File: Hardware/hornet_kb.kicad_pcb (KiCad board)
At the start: 2 copper layers, 195.1 x 100.9 mm, 149 parts, among them J1 Conn_ST_STDC14, J10 USB_C_Receptacle_USB2.0, J2 Conn_01x03, SW1 ESC, SW10 TAB, SW11 Q, SW12 W, SW13 E, SW14 R, SW15 T, SW17 M1, SW18 CAPS, SW19 A, SW2 `, SW20 S, SW21 D, SW22 F, SW23 G, SW25 M2, SW26 M3, SW27 SW_DPDT_x2, SW28 SHIFT, SW29 CTRL, SW3 1, SW30 Rot_Enc, SW31 Z, SW32 WIN, SW34 X, SW35 FN, SW37 C, SW38 ALT, SW4 2, SW40 V, SW41 SPACE, SW43 B, SW44 DEL, SW5 3, SW6 4, SW7 5, SW8 6, SW9 M0, SW98 SW_Push, U1 nRF52840, U2 BQ24040, U3 BQ51050BRHL, U4 AP22814BW5, U5 TPS2116DRL, Y1 32.768kHz, Y2 32MHz

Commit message: Finished draft placement of parts
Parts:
- removed R11: 1k, Resistor_SMD:R_0603_1608Metric
- removed R17: 20k, Resistor_SMD:R_0603_1608Metric
- removed Y2: 32MHz, Crystal:Crystal_SMD_2016-4Pin_2.0x1.6mm
- added D33: LED, LED_SMD:LED_0805_2012Metric, F.Cu at (208.2, 78.0)
- added IFA1: ~, RF_Antenna:Texas_SWRA117D_2.4GHz_Right, F.Cu at (223.2, 96.4)
- added Y3: Crystal_GND24, Crystal:Crystal_SMD_2016-4Pin_2.0x1.6mm, F.Cu at (225.6, 84.6)
- JP2: moved to B.Cu
- moved R16 94.6 mm to (212.3, 91.4), turned to 90 degrees
- moved C8 94.5 mm to (204.0, 98.5)
- moved L3 76.3 mm to (214.7, 75.6), turned to -90 degrees
- moved C25 72.6 mm to (221.5, 54.7), turned to 180 degrees
- moved D99 72.1 mm to (202.8, 77.8), turned to 90 degrees
- moved C14 71.2 mm to (209.5, 104.0)
- moved C15 70.8 mm to (205.2, 104.0)
- moved C16 69.3 mm to (207.5, 100.7), turned to 0 degrees
- moved R6 69.0 mm to (203.3, 73.6), turned to -90 degrees
- moved C13 68.9 mm to (203.4, 100.8)
- moved C24 68.8 mm to (207.0, 57.1), turned to -90 degrees
- moved C19 68.4 mm to (208.9, 91.4)
- moved C27 68.0 mm to (203.3, 91.4), turned to -90 degrees
- moved C20 67.6 mm to (206.0, 91.4)
- moved U3 67.2 mm to (208.5, 96.2)
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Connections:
- C28 pad 2: VSS_pa -> VSS_PA
- C29 pad 2: GND -> VSS_PA
- NT1 pad 1: VSS_pa -> VSS_PA
- R13 pad 1: NRF_ANTENNA -> Net-(IFA1-ANT)
- U1 pad AC21: /R_COL_2 -> unconnected-(U1-P0.25-PadAC21)
- U1 pad AD10: /R_COL_7 -> unconnected-(U1-P0.15-PadAD10)
- U1 pad AD12: /R_COL_6 -> unconnected-(U1-P0.17-PadAD12)
- U1 pad AD16: /R_ROW_2 -> unconnected-(U1-P0.20-PadAD16)
- U1 pad AD18: /R_COL_5 -> unconnected-(U1-P0.22-PadAD18)
- U1 pad AD20: /R_COL_4 -> unconnected-(U1-P0.24-PadAD20)
- U1 pad AD8: /R_ROW_0 -> unconnected-(U1-P0.13-PadAD8)
- U1 pad F23: VSS_pa -> VSS_PA
- U1 pad G1: /R_COL_1 -> unconnected-(U1-P0.26-PadG1)
- U1 pad H2: /R_COL_0 -> unconnected-(U1-P0.27-PadH2)
- U1 pad P2: /Rotary_L -> unconnected-(U1-P1.08-PadP2)
- U1 pad P23: /Rotary_R -> unconnected-(U1-P1.07-PadP23)
- U1 pad R1: /Rotary_SW -> unconnected-(U1-TRACEDATA3/P1.09-PadR1)
- U1 pad T23: /R_ROW_4 -> unconnected-(U1-P1.05-PadT23)
- U1 pad U24: /R_ROW_3 -> unconnected-(U1-P1.04-PadU24)
- U1 pad W24: /R_ROW_1 -> unconnected-(U1-P1.02-PadW24)
- U5 pad 1: Net-(U5-GND) -> GND
- U5 pad 4: Net-(U5-PR1) -> VBUS
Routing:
- net GND: track 0.00 -> 42.6 mm
- net Net-(C13-Pad1): track 0.00 -> 38.0 mm
- net VBUS: track 0.00 -> 23.9 mm, vias 0 -> 2
- net Net-(U3-AC2): track 0.00 -> 23.9 mm
- net VDDH: track 0.00 -> 16.3 mm
- net VDD: track 0.00 -> 11.3 mm
- net Net-(U1-XC1): track 0.00 -> 7.42 mm
- net /ANT: track 0.00 -> 7.23 mm
- net Net-(U1-DEC1): track 0.00 -> 7.07 mm
- net Net-(C29-Pad1): track 0.00 -> 6.23 mm
- net Net-(U1-XL1/P0.00): track 0.00 -> 6.23 mm
- net Net-(U1-XL2/P0.01): track 0.00 -> 6.09 mm
- net Net-(U1-XC2): track 0.00 -> 5.94 mm
- net Net-(U1-DEC4): track 0.00 -> 4.58 mm
- net Net-(U1-DCCH): track 0.00 -> 3.36 mm
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- added copper zone on In1.Cu, net VBUS
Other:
- board size 195.1 x 100.9 mm -> 193 x 100.3 mm
- copper layers 2 -> 4

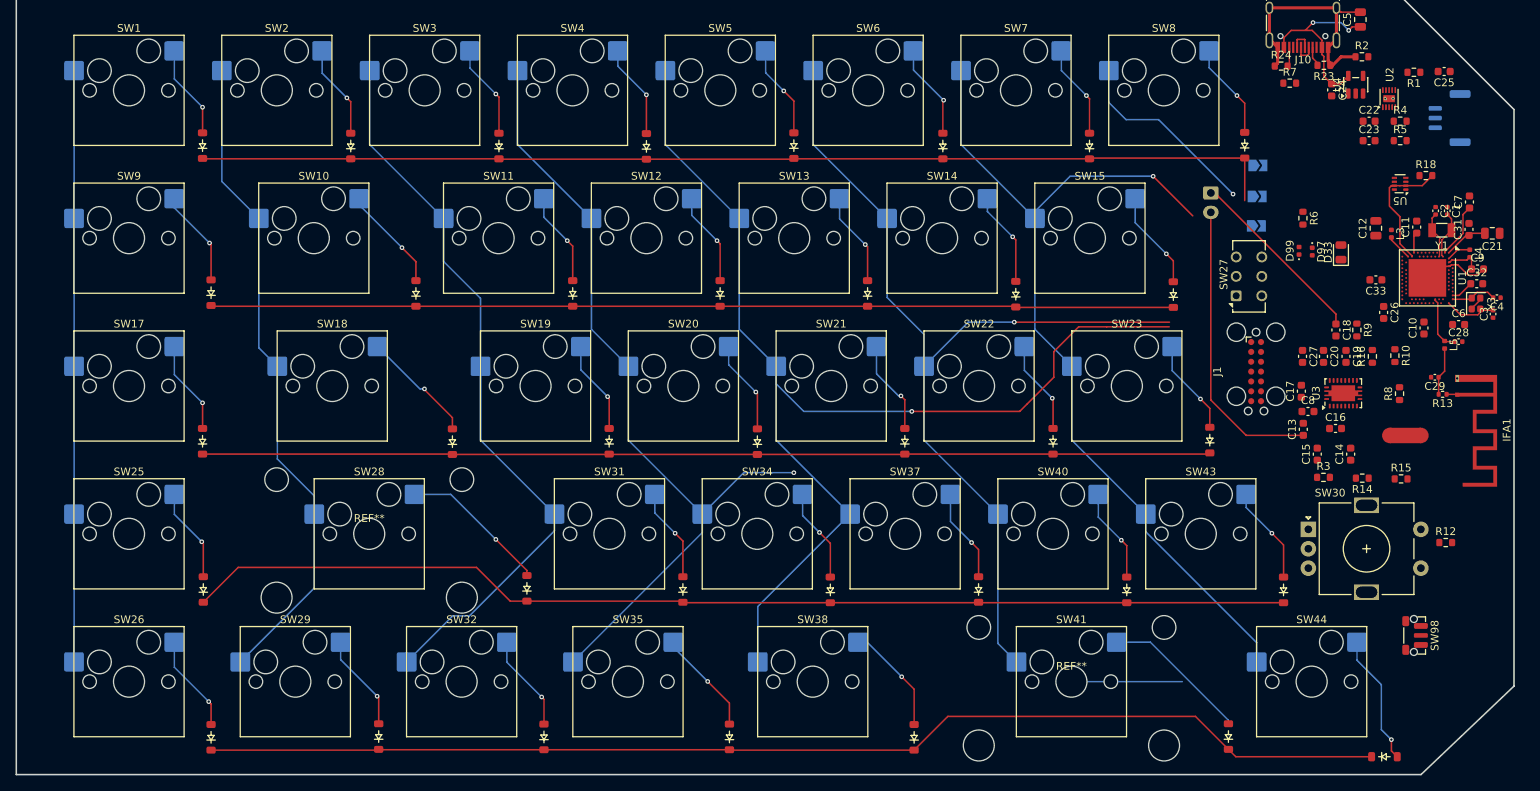
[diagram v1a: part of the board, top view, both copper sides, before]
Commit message: Update footprints and positions for multiple components
Changed footprints, positions, and orientations for several components including LEDs, capacitors, net ties, ICs, and antenna in hornet_kb.kicad_pcb. These updates improve layout accuracy and reflect changes in component selection and placement for better manufacturability and electrical performance.
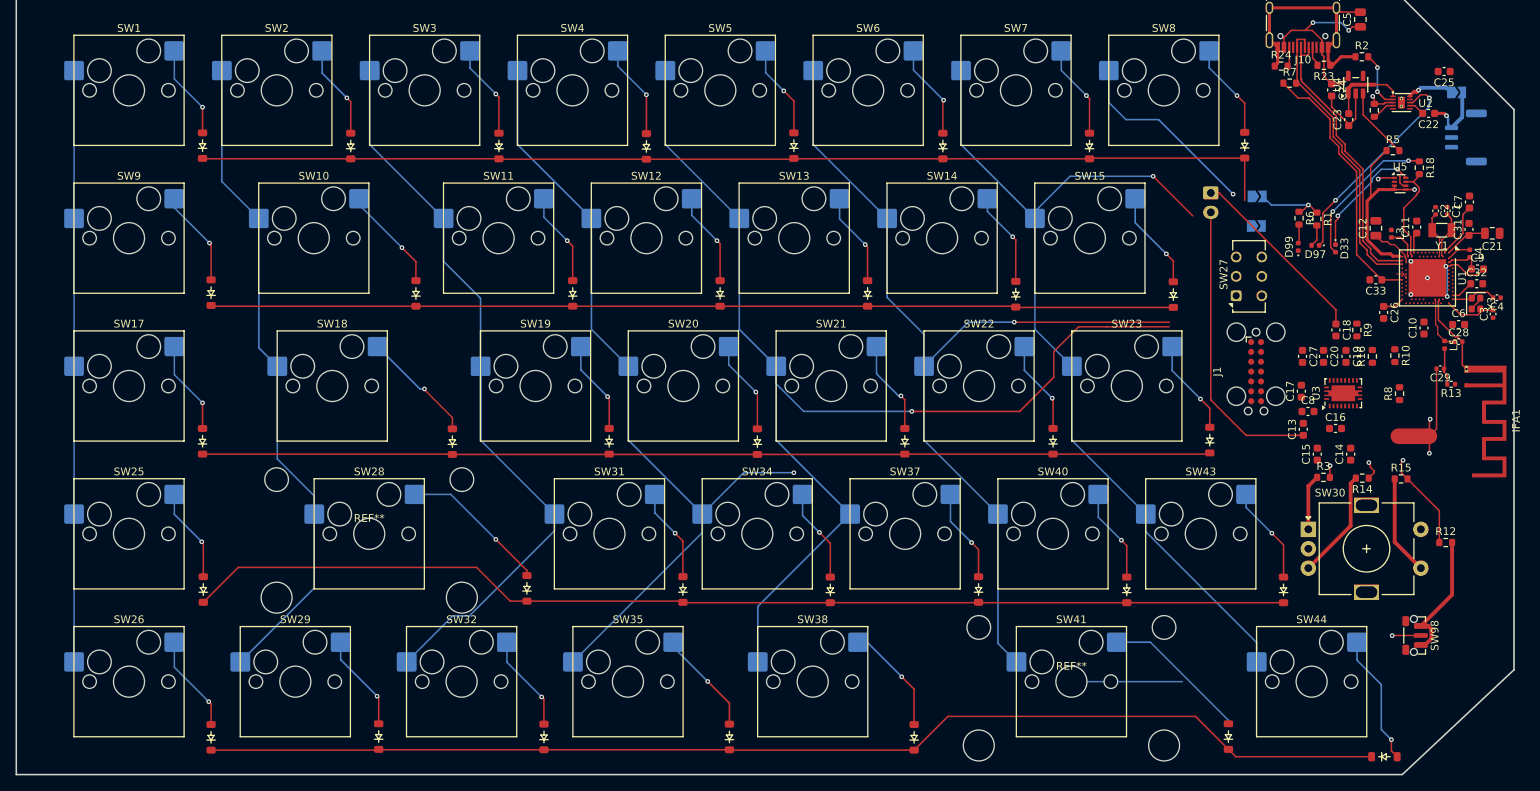
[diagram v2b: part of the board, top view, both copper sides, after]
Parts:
- D33: footprint LED_SMD:LED_0805_2012Metric -> LED_SMD:LED_0402_1005Metric
- moved JP2 27.3 mm to (223.1, 57.4)
- moved R1 22.7 mm to (205.1, 73.7), turned to -90 degrees
- moved C22 7.74 mm to (219.5, 60.1), turned to 180 degrees
- moved C23 3.77 mm to (209.2, 60.9), turned to 90 degrees
- moved R4 3.62 mm to (212.5, 59.7), turned to -90 degrees
- moved J2 3.26 mm to (224.3, 63.2)
- moved R13 1.70 mm to (222.4, 95.0)
- moved IFA1 1.70 mm to (224.4, 95.2)
- moved U2 1.68 mm to (216.0, 58.7), turned to 0 degrees
- moved R5 1.59 mm to (214.9, 64.9)
- moved R18 1.32 mm to (218.3, 67.1), turned to -90 degrees
- moved C29 1.30 mm to (221.0, 93.0)
- moved NT1 1.10 mm to (217.6, 101.7)
- moved D97 0.89 mm to (204.9, 77.1), turned to 180 degrees
- moved D33 0.86 mm to (207.5, 77.5), turned to -90 degrees
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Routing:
- net VDD: track 11.3 -> 64.9 mm, vias 0 -> 3
- net GND: track 42.6 -> 79.8 mm, vias 0 -> 8
- net /D+: track 2.99 -> 38.8 mm
- net /D-: track 2.93 -> 37.7 mm
- net Net-(D97-K): track 0.00 -> 28.0 mm, vias 0 -> 2
- net VBUS: track 23.9 -> 48.4 mm, vias 2 -> 3
- net VSS_PA: track 0.00 -> 24.2 mm, vias 0 -> 2
- net Net-(D33-A): track 0.00 -> 19.5 mm, vias 0 -> 2
- net /~{RESET}: track 0.00 -> 18.3 mm
- net +BATT: track 0.00 -> 18.0 mm, vias 0 -> 2
- net Net-(D33-K): track 0.00 -> 15.8 mm, vias 0 -> 2
- net /Rotary_R: track 0.00 -> 14.1 mm
- net /Rotary_SW: track 0.00 -> 12.9 mm
- net Net-(U2-IN): track 0.00 -> 10.2 mm
- net Net-(U4-~{FLG}): track 0.00 -> 9.32 mm
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- added copper zone on In2.Cu, net GND
- added copper zone on In2.Cu, net VSS_PA
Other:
- outline, holes or cut-outs redrawn

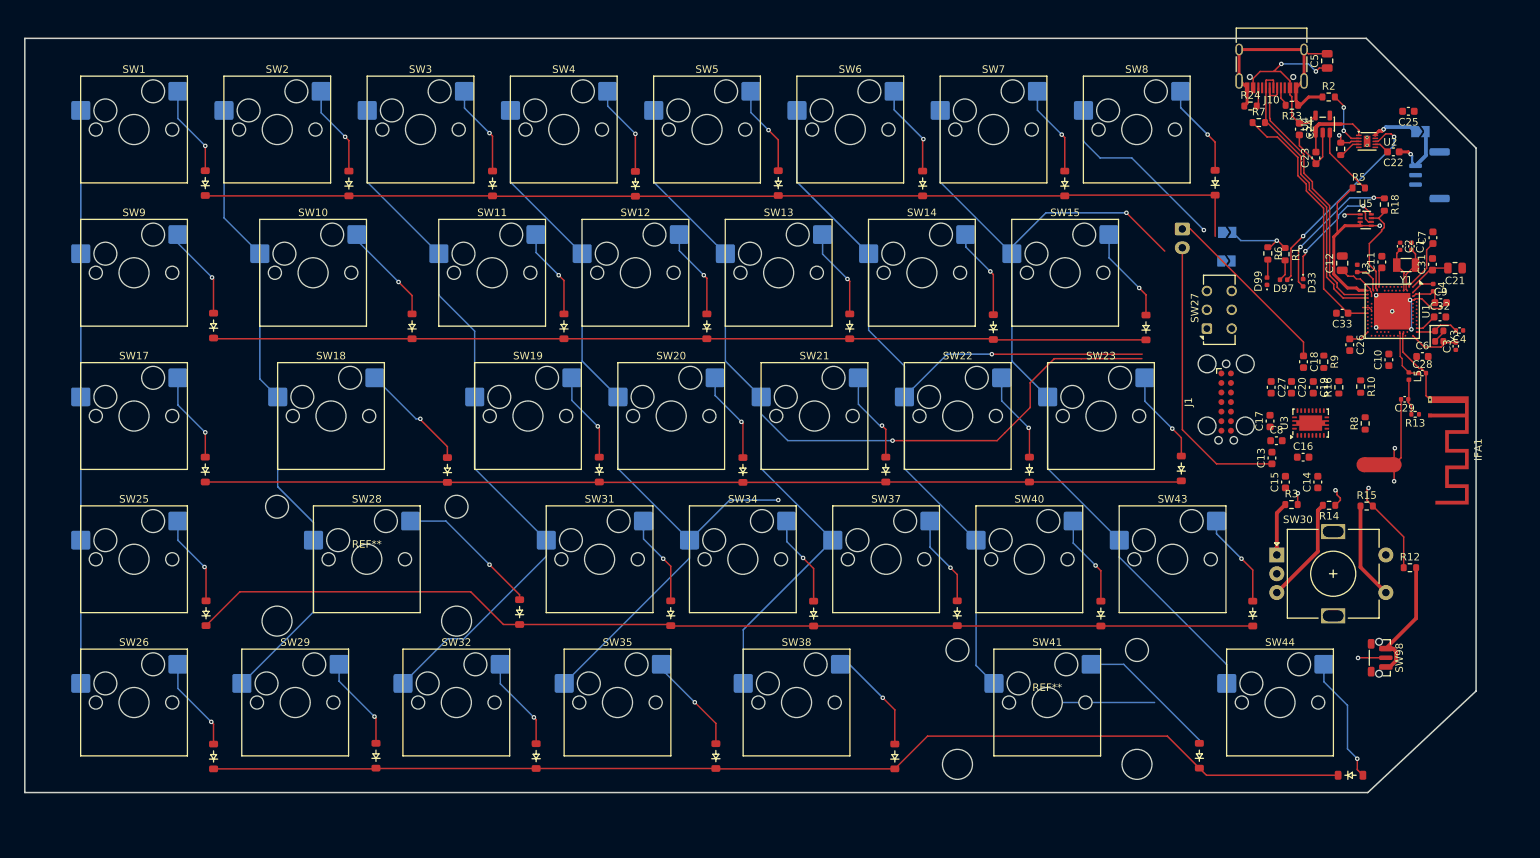
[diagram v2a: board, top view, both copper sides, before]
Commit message: Completed mcu routing
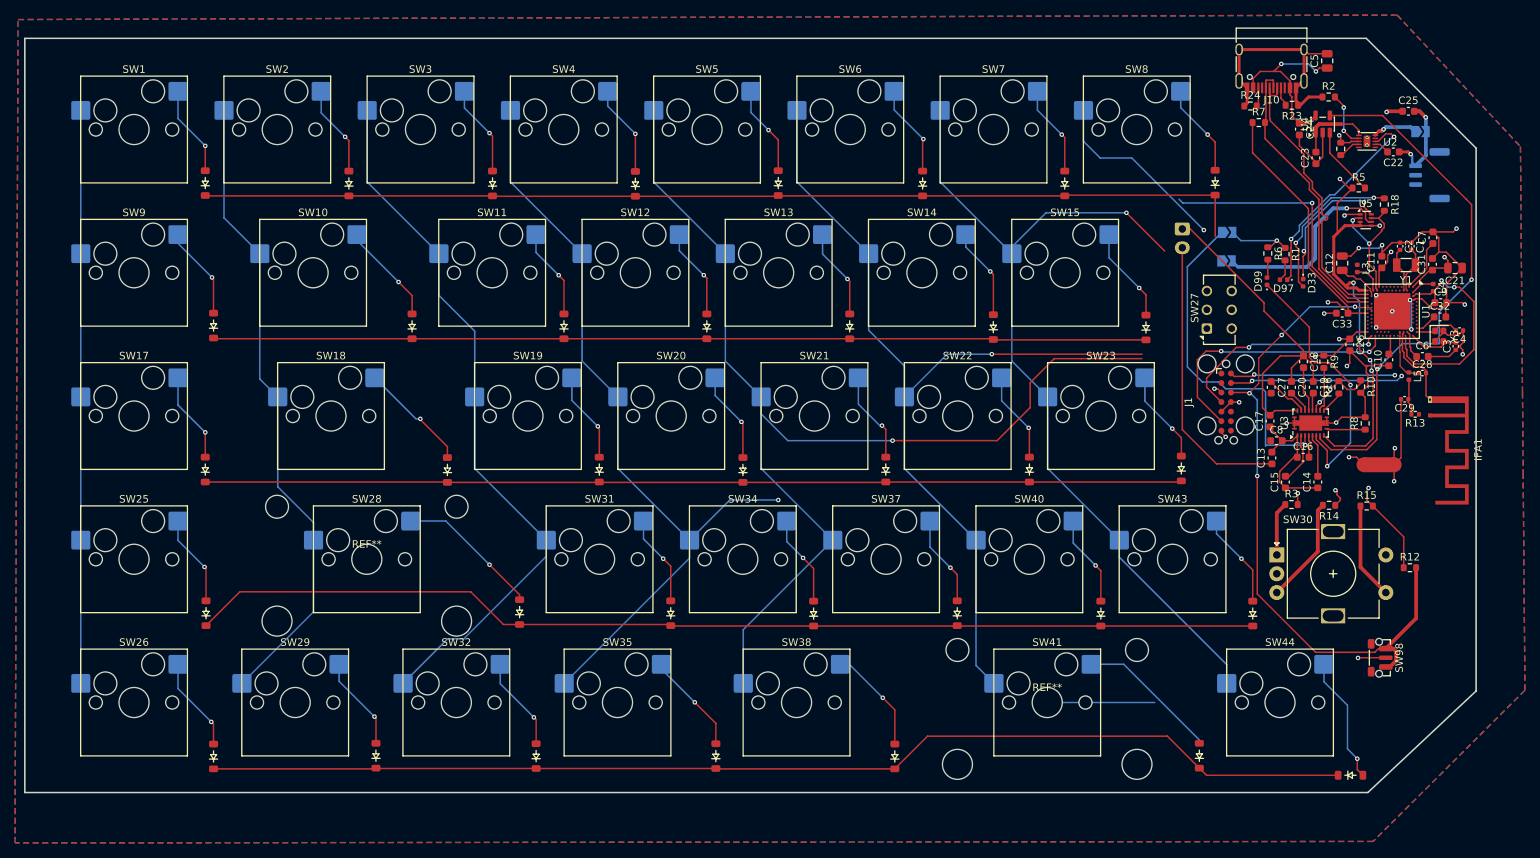
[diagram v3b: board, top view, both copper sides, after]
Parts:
- turned C25 to 0 degrees
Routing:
- net GND: track 79.8 -> 169.1 mm, vias 8 -> 21
- net Net-(U3-~{AD-EN}): track 0.00 -> 72.3 mm, vias 0 -> 2
- net /~{RESET}: track 18.3 -> 90.5 mm, vias 0 -> 4
- net Net-(JP3-A): track 0.00 -> 45.4 mm, vias 0 -> 1
- net Net-(D99-K): track 0.00 -> 35.8 mm, vias 0 -> 2
- net unconnected-(U1-P0.13-PadAD8): track 0.00 -> 35.7 mm, vias 0 -> 1
- net /PRG_CLK: track 0.00 -> 35.3 mm, vias 0 -> 2
- net VBUS: track 48.4 -> 81.1 mm, vias 3 -> 8
- net /PRC_DIO: track 0.00 -> 29.0 mm, vias 0 -> 2
- net Net-(U1-DEC4): track 4.58 -> 31.2 mm, vias 0 -> 2
- net Net-(U3-AC2): track 24.2 -> 48.5 mm
- net +VDC: track 2.11 -> 25.8 mm, vias 0 -> 1
- net /COMPRT_RX: track 0.00 -> 23.1 mm, vias 0 -> 2
- net /COMPRT_TX: track 0.00 -> 22.1 mm, vias 0 -> 2
- net Net-(U3-AC1): track 0.00 -> 19.8 mm
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- added copper zone on B.Cu, net GND
- added copper zone on F.Cu, net GND
- added copper zone on In1.Cu, net VDD

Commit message: FINISHED FIRST DRAFT OF LAYOUT!!
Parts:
- added JP4: PWR_SWITCH, Jumper:SolderJumper-2_P1.3mm_Open_TrianglePad1.0x1.5mm, B.Cu at (191.9, 78.2)
- SW27: footprint Button_Switch_THT:SW_CK_JS202011CQN_DPDT_Straight -> ScottoKeebs_Miscellaneous:SW_CK_JS202011CQN_DPDT_Straight
- moved JP1 9.39 mm to (204.6, 68.7)
- moved D99 7.36 mm to (209.0, 81.1)
- moved R6 6.25 mm to (206.0, 79.0), turned to -45 degrees
- moved D97 4.12 mm to (208.5, 79.1), turned to -45 degrees
- moved D33 2.73 mm to (210.0, 78.6), turned to -45 degrees
- moved JP3 2.51 mm to (198.4, 68.5)
- moved J1 2.35 mm to (197.3, 95.7)
- moved R1 1.61 mm to (205.9, 75.1)
- moved SW27 1.14 mm to (195.0, 84.7)
- moved L1 0.16 mm to (191.5, 70.2)
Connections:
- D10 pad 1: /R_ROW_2 -> /R_ROW_1
- D11 pad 1: /R_ROW_2 -> /R_ROW_1
- D12 pad 1: /R_ROW_2 -> /R_ROW_1
- D13 pad 1: /R_ROW_2 -> /R_ROW_1
- D14 pad 1: /R_ROW_2 -> /R_ROW_1
- D15 pad 1: /R_ROW_2 -> /R_ROW_1
- D17 pad 1: /R_ROW_1 -> /R_ROW_2
- D18 pad 1: /R_ROW_1 -> /R_ROW_2
- D19 pad 1: /R_ROW_1 -> /R_ROW_2
- D20 pad 1: /R_ROW_1 -> /R_ROW_2
- D21 pad 1: /R_ROW_1 -> /R_ROW_2
- D22 pad 1: /R_ROW_1 -> /R_ROW_2
- D23 pad 1: /R_ROW_1 -> /R_ROW_2
- D9 pad 1: /R_ROW_2 -> /R_ROW_1
- U1 pad A14: unconnected-(U1-P1.15-PadA14) -> /Rotary_SW
- U1 pad A16: unconnected-(U1-P1.13-PadA16) -> /Rotary_R
- U1 pad A20: unconnected-(U1-P1.10-PadA20) -> /Rotary_L
- U1 pad A8: unconnected-(U1-AIN7/P0.31-PadA8) -> /R_ROW_3
- U1 pad AD16: unconnected-(U1-P0.20-PadAD16) -> /R_ROW_0
- U1 pad AD18: unconnected-(U1-P0.22-PadAD18) -> /R_COL_6
- U1 pad AD20: unconnected-(U1-P0.24-PadAD20) -> /R_COL_5
- U1 pad AD22: unconnected-(U1-TRACEDATA0/P1.00-PadAD22) -> /R_COL_4
- U1 pad AD8: unconnected-(U1-P0.13-PadAD8) -> /R_COL_7
- U1 pad J1: unconnected-(U1-AIN2/P0.04-PadJ1) -> /R_COL_0
- U1 pad J24: unconnected-(U1-NFC2/P0.10-PadJ24) -> /COMPRT_RX
- U1 pad L1: unconnected-(U1-P0.06-PadL1) -> /R_COL_1
- U1 pad L24: unconnected-(U1-NFC1/P0.09-PadL24) -> /COMPRT_TX
- U1 pad N1: unconnected-(U1-P0.08-PadN1) -> /R_COL_2
- U1 pad R24: unconnected-(U1-P1.06-PadR24) -> /R_ROW_2
- U1 pad U24: unconnected-(U1-P1.04-PadU24) -> /R_COL_3
- U1 pad W24: unconnected-(U1-P1.02-PadW24) -> /R_ROW_1
- U1 pad Y23: unconnected-(U1-P1.01-PadY23) -> /R_ROW_4
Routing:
- net /R_COL_0: track 76.2 -> 278.8 mm, vias 0 -> 5
- net /R_COL_1: track 85.1 -> 266.9 mm, vias 0 -> 5
- net /R_COL_2: track 104.7 -> 265.9 mm, vias 0 -> 5
- net /R_COL_3: track 107.0 -> 208.4 mm, vias 1 -> 5
- net +BATT: track 21.8 -> 121.7 mm, vias 3 -> 7
- net /R_ROW_4: track 153.6 -> 243.0 mm, vias 0 -> 2
- net /R_ROW_3: track 143.0 -> 213.3 mm, vias 0 -> 2
- net /R_ROW_2: track 124.1 -> 180.4 mm, vias 0 -> 2
- net /R_COL_4: track 151.8 -> 203.5 mm, vias 1 -> 2
- net /Rotary_SW: track 12.9 -> 63.5 mm, vias 0 -> 1
- net /Rotary_R: track 14.1 -> 63.5 mm, vias 0 -> 1
- net /Rotary_L: track 7.17 -> 51.7 mm, vias 0 -> 1
- net /R_COL_5: track 121.0 -> 158.7 mm
- net unconnected-(U1-P0.13-PadAD8): track 35.7 -> 0.00 mm, vias 1 -> 0
- net /R_COL_6: track 117.2 -> 149.6 mm
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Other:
- outline, holes or cut-outs redrawn
- board text removed: "Try and make this space as small as possible"
